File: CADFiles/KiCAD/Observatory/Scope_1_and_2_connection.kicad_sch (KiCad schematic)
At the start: 0 parts

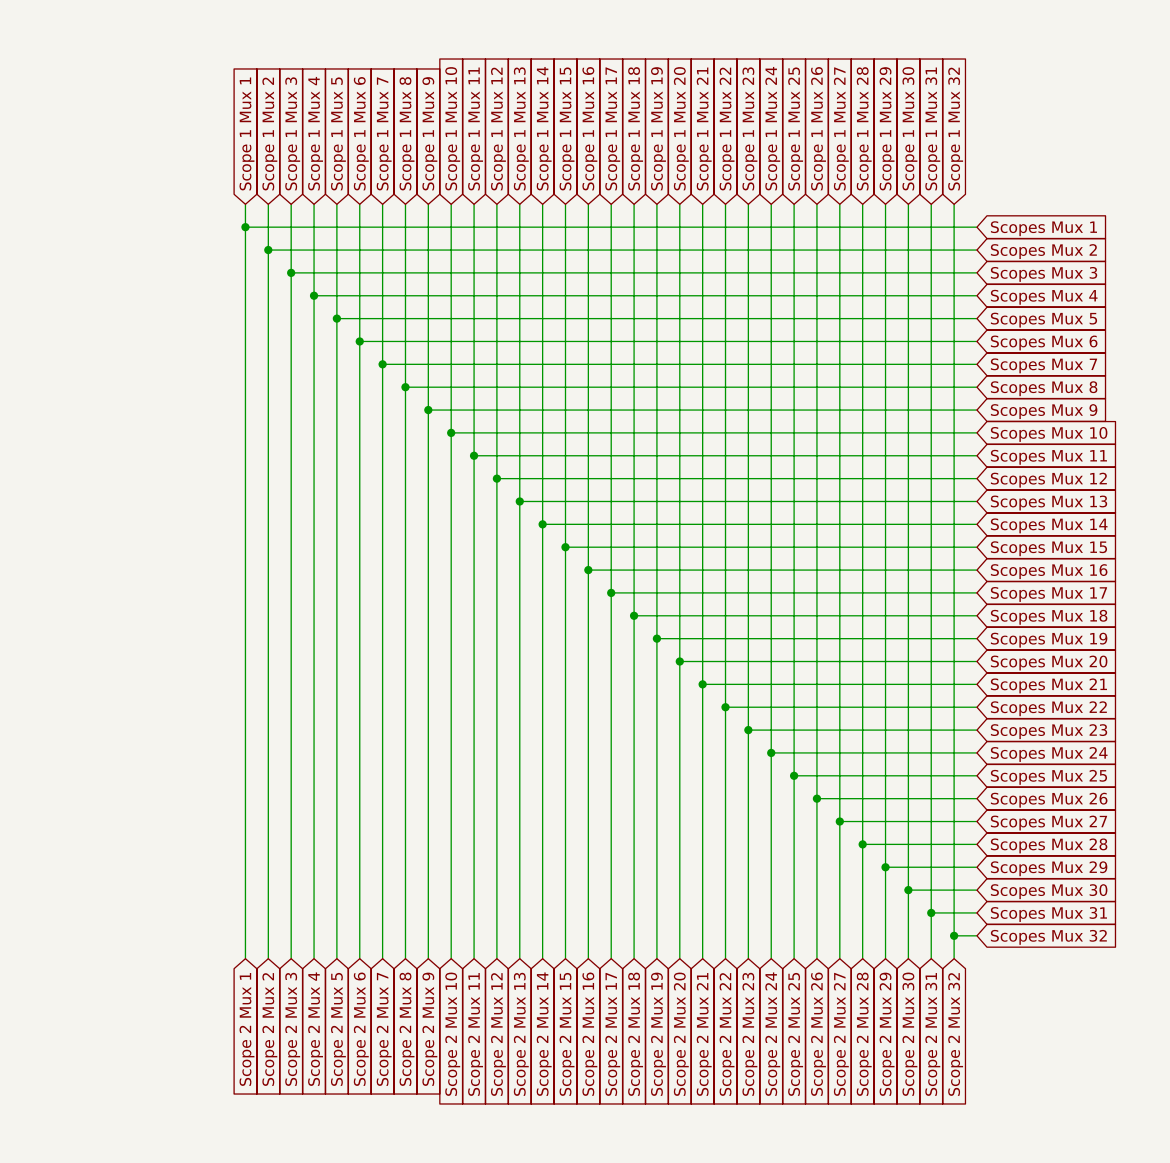
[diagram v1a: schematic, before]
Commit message: All nets routed.
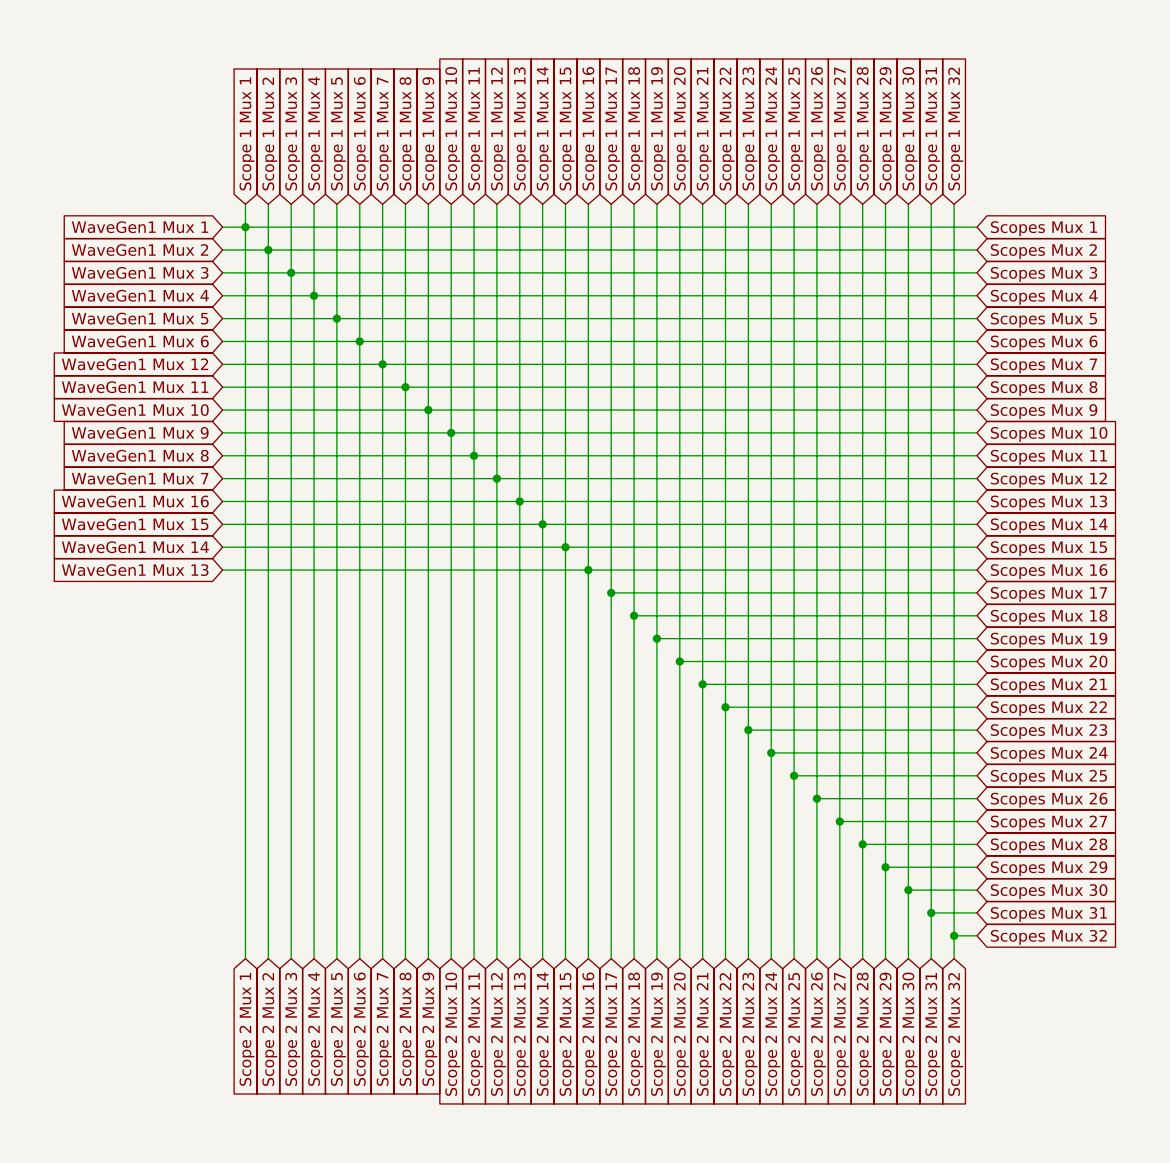
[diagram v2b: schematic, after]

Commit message: AD DC(-) error fixed. Jumpers added for feet grounds and DC supplies
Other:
- company: (none) -> West Lab
- title: (none) -> SCuM Observatory
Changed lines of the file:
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@@
 	(generator_version "9.0")
 	(paper "A4")
+	(title_block
+		(title "SCuM Observatory")
+		(date "2025-03-21")
+		(rev "2")
+		(company "West Lab")
+	)
 	(junction
 		(at 78.74 80.01)
